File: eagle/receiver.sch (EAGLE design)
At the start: 18 parts, among them IC1 7805TV, Q1 16 Mhz, U1 ATMEGA328P-PU

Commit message: Fixed reversed DC power jack and finished PCB
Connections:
- removed net N$8: 9V-JACK.RING, JP5.2
- new net N$7: 9V-JACK.TIP, JP5.2
- net GND: now also 9V-JACK.RING; no longer 9V-JACK.TIP
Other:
- moved on the sheet: 9V-JACK
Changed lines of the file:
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@@
 <instance part="R1" gate="G$1" x="40.64" y="68.58" rot="R90"/>
 <instance part="R2" gate="G$1" x="101.6" y="2.54" rot="R90"/>
-<instance part="9V-JACK" gate="G$1" x="-25.4" y="63.5" rot="MR180"/>
+<instance part="9V-JACK" gate="G$1" x="-25.4" y="63.5"/>
 <instance part="GND2" gate="1" x="10.16" y="53.34"/>
 <instance part="GND3" gate="1" x="73.66" y="7.62"/>
@@
 <wire x1="25.4" y1="68.58" x2="25.4" y2="60.96" width="0.1524" layer="91"/>
 <junction x="25.4" y="60.96"/>
-<pinref part="9V-JACK" gate="G$1" pin="TIP"/>
+<pinref part="9V-JACK" gate="G$1" pin="RING"/>
 <wire x1="-20.32" y1="60.96" x2="-5.08" y2="60.96" width="0.1524" layer="91"/>
 <junction x="-5.08" y="60.96"/>
@@
 </segment>
 </net>
-<net name="N$8" class="1">
-<segment>
-<pinref part="9V-JACK" gate="G$1" pin="RING"/>
-<wire x1="-20.32" y1="66.04" x2="-20.32" y2="73.66" width="0.1524" layer="91"/>
-<pinref part="JP5" gate="A" pin="2"/>
-</segment>
-</net>
 <net name="IR" class="0">
 <segment>
@@
 </segment>
 </net>
+<net name="N$7" class="1">
+<segment>
+<pinref part="9V-JACK" gate="G$1" pin="TIP"/>
+<pinref part="JP5" gate="A" pin="2"/>
+<wire x1="-20.32" y1="66.04" x2="-20.32" y2="73.66" width="0.1524" layer="91"/>
+</segment>
+</net>

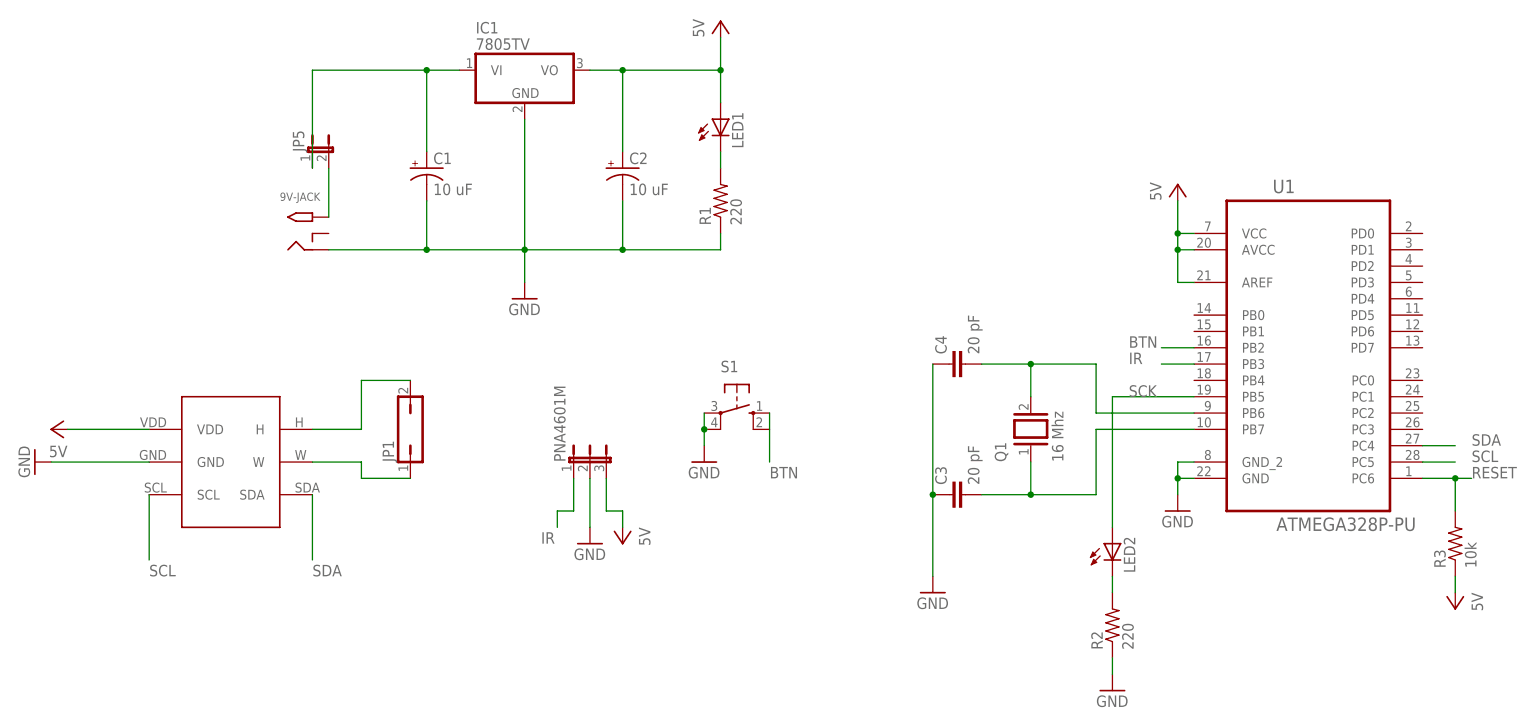
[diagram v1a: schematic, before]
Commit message: Removed dpot from project and replaced with single input MUX
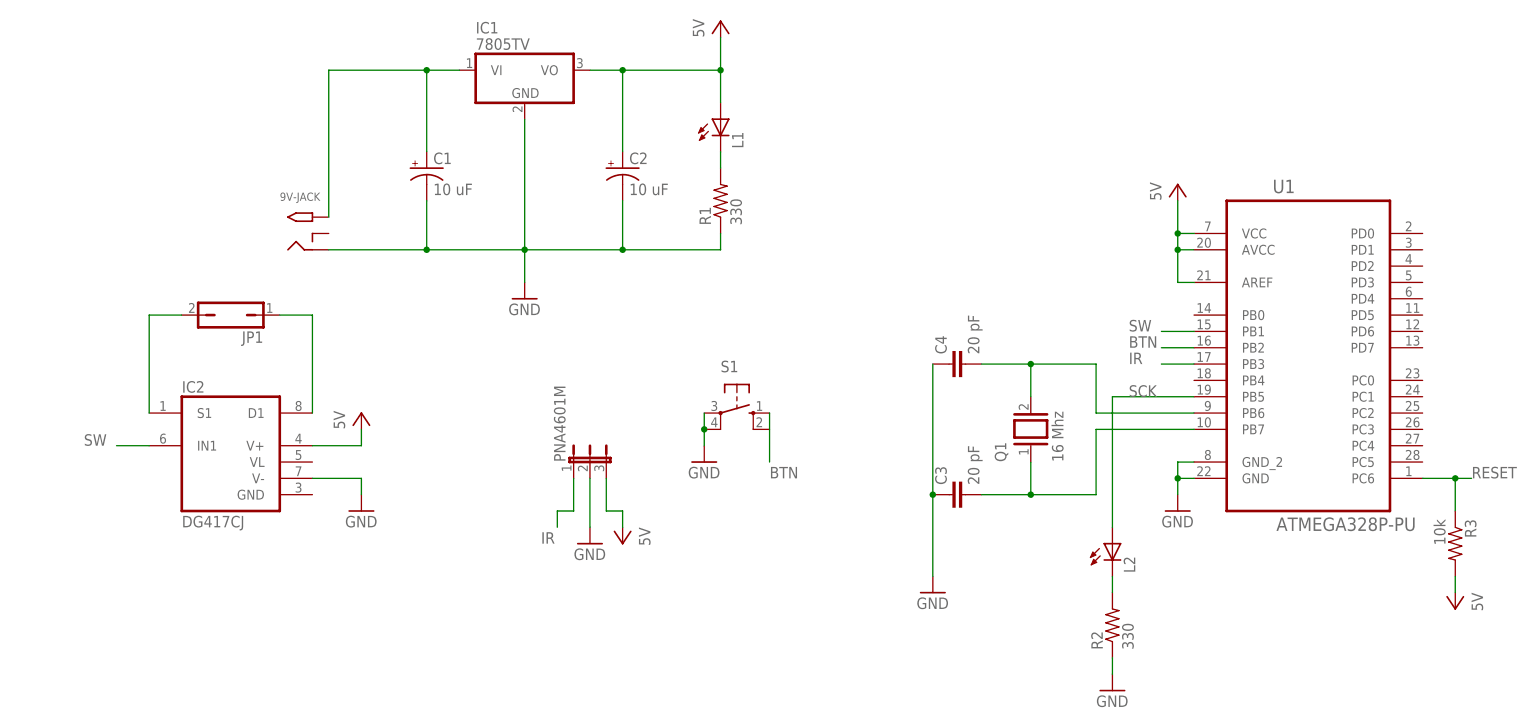
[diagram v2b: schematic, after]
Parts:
- removed JP5: (no value), jumper:JP1E
- removed LED1, LED2: (no value), adafruit:LED5MM
- removed U$1: TPL0401B, tpl0401b:TPL0401B
- added IC2: DG417CJ, maxim:DG417CJ
- added L1, L2: (no value), EE445L:LED3MM
- R1, R2: value 220 -> 330
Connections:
- removed net N$1: C1.+, IC1.VI, JP5.1
- removed net SCL: U$1.SCL, U1.PC5
- removed net SDA: U$1.SDA, U1.PC4
- new net SW: IC2.IN1, U1.PB1
- net 5V: now also IC2.V+, L1.A, R3.2; no longer LED1.A, R3.1, U$1.VDD
- net GND: now also IC2.V-; no longer U$1.GND
- net N$2: now also L1.C; no longer LED1.C
- net N$3: now also IC2.S1, JP1.2; no longer JP1.1, U$1.W
- net N$6: now also IC2.D1, JP1.1; no longer JP1.2, U$1.H
- net N$7: now also C1.+, IC1.VI; no longer JP5.2
- net N$9: now also L2.C; no longer LED2.C
- net RESET: now also R3.1; no longer R3.2
- net SCK: now also L2.A; no longer LED2.A
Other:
- moved on the sheet: JP1, R3
